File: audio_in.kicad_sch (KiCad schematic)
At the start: 12 parts, among them J4 JST SH3, J5 Header_2x1, U2 OPA1678

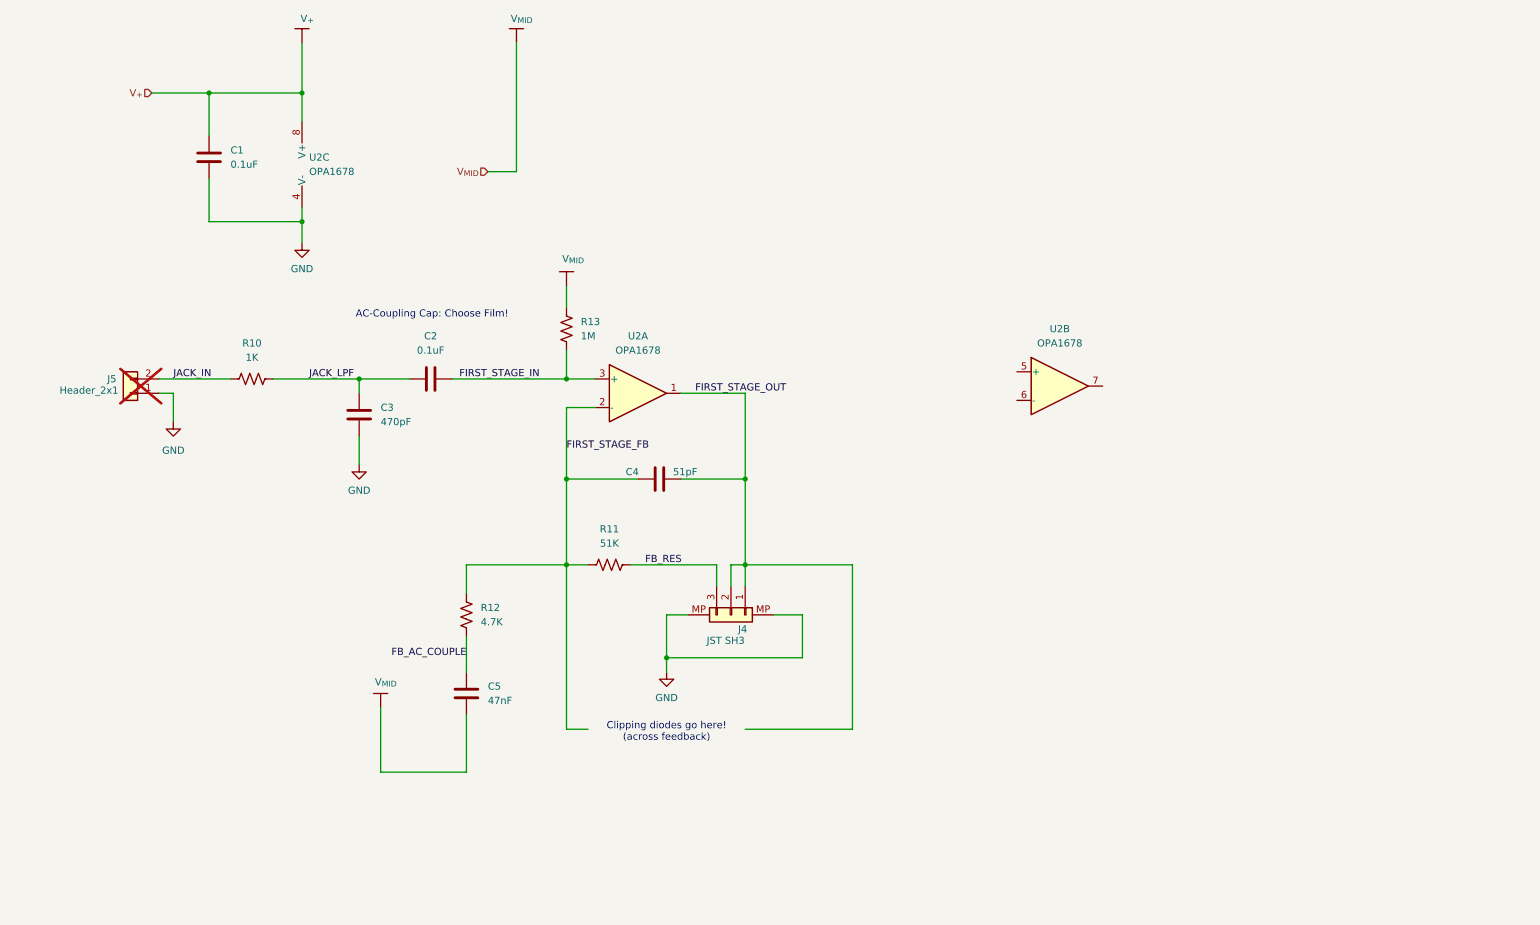
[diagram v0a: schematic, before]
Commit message: Finished second stage, added diode clipping options, and started current buffer.
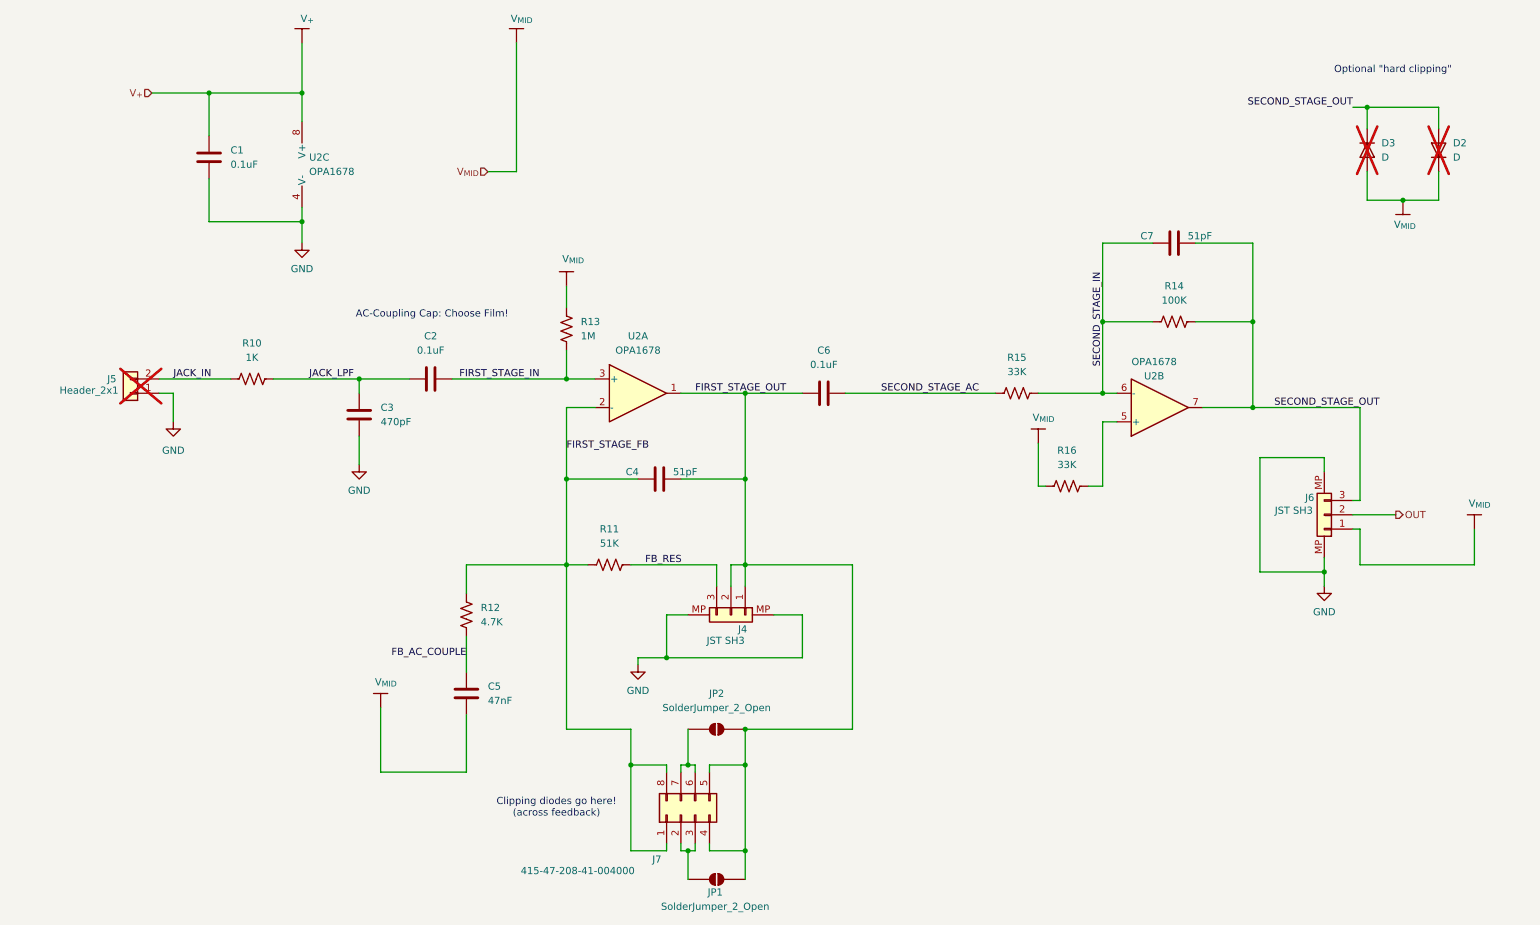
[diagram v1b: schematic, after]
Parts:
- added C6: 0.1uF, Capacitor_SMD:C_1210_3225Metric, symbol #inventree_kicad:C_0U1_PEN_50V_1210
- added C7: 51pF, Capacitor_SMD:C_0402_1005Metric, symbol #inventree_kicad:C_51P_NP0_50V_0402
- added D2, D3: D, symbol Device:D
- added J6: JST SH3, Connector_JST:JST_SH_BM03B-SRSS-TB_1x03-1MP_P1.00mm_Vertical, symbol #inventree_kicad:PWR_CONN_3PIN_JST_SH3_VERT_SMD
- added J7: 415-47-208-41-004000, Connector_PinSocket_2.54mm:PinSocket_2x04_P2.54mm_Vertical, symbol #inventree_kicad:PWR_CONN_8_PIN_SOCKET_THRU
- added JP1, JP2: SolderJumper_2_Open, Jumper:SolderJumper-2_P1.3mm_Open_TrianglePad1.0x1.5mm, symbol Jumper:SolderJumper_2_Open
- added R14: 100K, Resistor_SMD:R_0402_1005Metric, symbol #inventree_kicad:R_100K_0402_1PCT_0W0625
- added R15, R16: 33K, Resistor_SMD:R_0402_1005Metric, symbol #inventree_kicad:R_33K_0402_1PCT_0W0625
- J4: footprint Connector_JST:JST_SH_SM03B-SRSS-TB_1x03-1MP_P1.00mm_Horizontal -> Connector_JST:JST_SH_BM03B-SRSS-TB_1x03-1MP_P1.00mm_Vertical
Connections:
- net FIRST_STAGE_FB: now also J7.1 (Pin_1), J7.8 (Pin_8)
- net FIRST_STAGE_OUT: now also C6.1, J7.4 (Pin_4), J7.5 (Pin_5), JP1.2 (B), JP2.2 (B)
- net GND: now also J6.MP
- net V_{MID}: now also D2.1 (K), D3.2 (A), J6.1 (Pin_1), R16.1
- net at U2.5 (+): now also R16.2
- net SECOND_STAGE_IN: now reaches U2.6 (-)
- net SECOND_STAGE_IN: now also C7.1, R14.1, R15.2
- net SECOND_STAGE_OUT: now reaches U2.7
- net SECOND_STAGE_OUT: now also C7.2, D2.2 (A), D3.1 (K), J6.3 (Pin_3), R14.2
- new net: J7.2 (Pin_2), J7.3 (Pin_3), JP1.1 (A)
- new net: J7.6 (Pin_6), J7.7 (Pin_7), JP2.1 (A)
- new net OUT: J6.2 (Pin_2)
- new net SECOND_STAGE_AC: C6.2, R15.1
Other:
- note added: "Optional "hard clipping""
- moved on the sheet: U2B

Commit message: Added notes and started work on boost converter.
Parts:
- D2, D3: footprint (none) -> Diode_SMD:D_SOD-123
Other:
- note added: "1N4148W-7-F"
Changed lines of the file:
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@@
+		)
+	)
+	(text "1N4148W-7-F"
+		(exclude_from_sim no)
+		(at 246.888 55.88 0)
+		(effects
+			(font
+				(size 1.27 1.27)
+			)
 		)
 	)
@@
 			)
 		)
-		(property "Footprint" ""
+		(property "Footprint" "Diode_SMD:D_SOD-123"
 			(at 271.78 54.61 0)
 			(hide yes)
@@
 			)
 		)
-		(property "Footprint" ""
+		(property "Footprint" "Diode_SMD:D_SOD-123"
 			(at 259.08 54.61 0)
 			(hide yes)

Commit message: Implemented boost stage and now working on schematics for current buffers and rail splitter.
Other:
- title: (none) -> ${PROJECT_NAME}
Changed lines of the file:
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@@
 	(generator_version "10.0")
 	(paper "A4")
+	(title_block
+		(title "${PROJECT_NAME}")
+		(date "2026-08-25")
+		(rev "${REVISION}")
+		(comment 1 "${PCBA_IPN}")
+	)
 	(text "Optional \"hard clipping\""
 		(exclude_from_sim no)

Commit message: Started working on watchdog circuit.
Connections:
- net SECOND_STAGE_OUT renamed WD_AUDIO_OUT
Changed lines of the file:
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@@
+	)
+	(junction
+		(at 257.81 100.33)
+		(diameter 0)
+		(color 0 0 0 0)
 	)
 	(junction
@@
 	(wire
 		(pts
+			(xy 257.81 100.33) (xy 266.7 100.33)
+		)
+		(stroke
+			(width 0)
+			(type default)
+		)
+	)
+	(wire
+		(pts
 			(xy 128.27 163.83) (xy 128.27 157.48)
 		)
@@
 		)
 	)
+	(hierarchical_label "WD_AUDIO_OUT"
+		(shape output)
+		(at 266.7 100.33 0)
+		(effects
+			(font
+				(size 1.27 1.27)
+			)
+			(justify left)
+		)
+	)

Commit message: Small tunes and adjustments before Inventree work.
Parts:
- added FB3: MDF2016BSS600CTD25, Inductor_SMD:L_Wuerth_PMFI-201610, symbol Device:FerriteBead
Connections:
- net V_{+}: now also FB3.1, FB3.2
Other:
- note added: "Av = -R14 / R15 => Av = -100K / 33K = -3.03x"
- note added: "Av = 1 + (R11 + R_pot) / R12 Av_min (R_pot = 0): => Av_min = 1 + 51K/4.7K = 11.9x (21.5 dB) Av_max (R_pot = 500K): => Av_max = 1 + (51K + 500K)/4.7K = 118.2x (41.5 dB)"
- note added: "Gain pot"
- note added: "Volume pot"
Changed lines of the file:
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@@
 	(title_block
 		(title "${PROJECT_NAME}")
-		(date "2026-08-25")
+		(date "2026-08-29")
 		(rev "${REVISION}")
 		(comment 1 "${PCBA_IPN}")
@@
 		)
 	)
+	(text "Gain pot"
+		(exclude_from_sim no)
+		(at 154.94 132.842 0)
+		(effects
+			(font
+				(size 1.27 1.27)
+			)
+		)
+	)
+	(text "Av = -R14 / R15\n=> Av = -100K / 33K = -3.03x"
+		(exclude_from_sim no)
+		(at 197.866 122.174 0)
+		(effects
+			(font
+				(size 1.27 1.27)
+			)
+			(justify left)
+		)
+	)
+	(text "Volume pot"
+		(exclude_from_sim no)
+		(at 265.43 113.284 0)
+		(effects
+			(font
+				(size 1.27 1.27)
+			)
+		)
+	)
 	(text "1N4148W-7-F"
 		(exclude_from_sim no)
@@
 		)
 	)
+	(text "Av = 1 + (R11 + R_pot) / R12\n\nAv_min (R_pot = 0):\n=> Av_min = 1 + 51K/4.7K = 11.9x (21.5 dB)\n\nAv_max (R_pot = 500K):\n=> Av_max = 1 + (51K + 500K)/4.7K = 118.2x (41.5 dB)"
+		(exclude_from_sim no)
+		(at 126.238 67.818 0)
+		(effects
+			(font
+				(size 1.27 1.27)
+			)
+			(justify left)
+		)
+	)
 	(junction
 		(at 116.84 113.03)
@@
 	)
 	(junction
+		(at 53.34 44.45)
+		(diameter 0)
+		(color 0 0 0 0)
+	)
+	(junction
 		(at 116.84 95.25)
 		(diameter 0)
@@
 	)
 	(junction
-		(at 53.34 44.45)
-		(diameter 0)
-		(color 0 0 0 0)
-	)
-	(junction
 		(at 134.62 144.78)
 		(diameter 0)
@@
 	(wire
 		(pts
-			(xy 43.18 44.45) (xy 53.34 44.45)
+			(xy 26.67 44.45) (xy 34.29 44.45)
 		)
 		(stroke
@@
 		(pts
 			(xy 116.84 113.03) (xy 129.54 113.03)
+		)
+		(stroke
+			(width 0)
+			(type default)
+		)
+	)
+	(wire
+		(pts
+			(xy 41.91 44.45) (xy 53.34 44.45)
 		)
 		(stroke
@@
 	(hierarchical_label "V_{+}"
 		(shape input)
-		(at 43.18 44.45 180)
+		(at 26.67 44.45 180)
 		(effects
 			(font
@@
 					(unit 1)
 				)
+			)
+		)
+	)
+	(symbol
+		(lib_id "Device:FerriteBead")
+		(at 38.1 44.45 90)
+		(unit 1)
+		(body_style 1)
+		(exclude_from_sim no)
+		(in_bom yes)
+		(on_board yes)
+		(in_pos_files yes)
+		(dnp no)
+		(fields_autoplaced yes)
+		(property "Reference" "FB3"
+			(at 38.0492 36.83 90)
+			(show_name no)
+			(do_not_autoplace no)
+			(effects
+				(font
+					(size 1.27 1.27)
+				)
+			)
+		)
+		(property "Value" "MDF2016BSS600CTD25"
+			(at 38.0492 39.37 90)
+			(show_name no)
+			(do_not_autoplace no)
+			(effects
+				(font
+					(size 1.27 1.27)
+				)
+			)
+		)
+		(property "Footprint" "Inductor_SMD:L_Wuerth_PMFI-201610"
+			(at 38.1 46.228 90)
+			(hide yes)
+			(show_name no)
+			(do_not_autoplace no)
+			(effects
+				(font
+					(size 1.27 1.27)
+				)
+			)
+		)
+		(property "Datasheet" ""
+			(at 38.1 44.45 0)
+			(hide yes)
+			(show_name no)
+			(do_not_autoplace no)
+			(effects
+				(font
+					(size 1.27 1.27)
+				)
+			)
+		)
+		(property "Description" "Ferrite bead"
+			(at 38.1 44.45 0)
+			(hide yes)
+			(show_name no)
+			(do_not_autoplace no)
+			(effects
+				(font
+					(size 1.27 1.27)
+				)
+			)
+		)
+		(pin "2"
+		)
+		(pin "1"
+		)
+		(instances
+			(project "headphone_amp"
+				(path "/62ffec33-ae93-49a8-bfe6-566578dd8e82/fdaed4ad-6382-4025-bc3e-39eb3bc4a0fb"
+					(reference "FB3")
+					(unit 1)
+				)

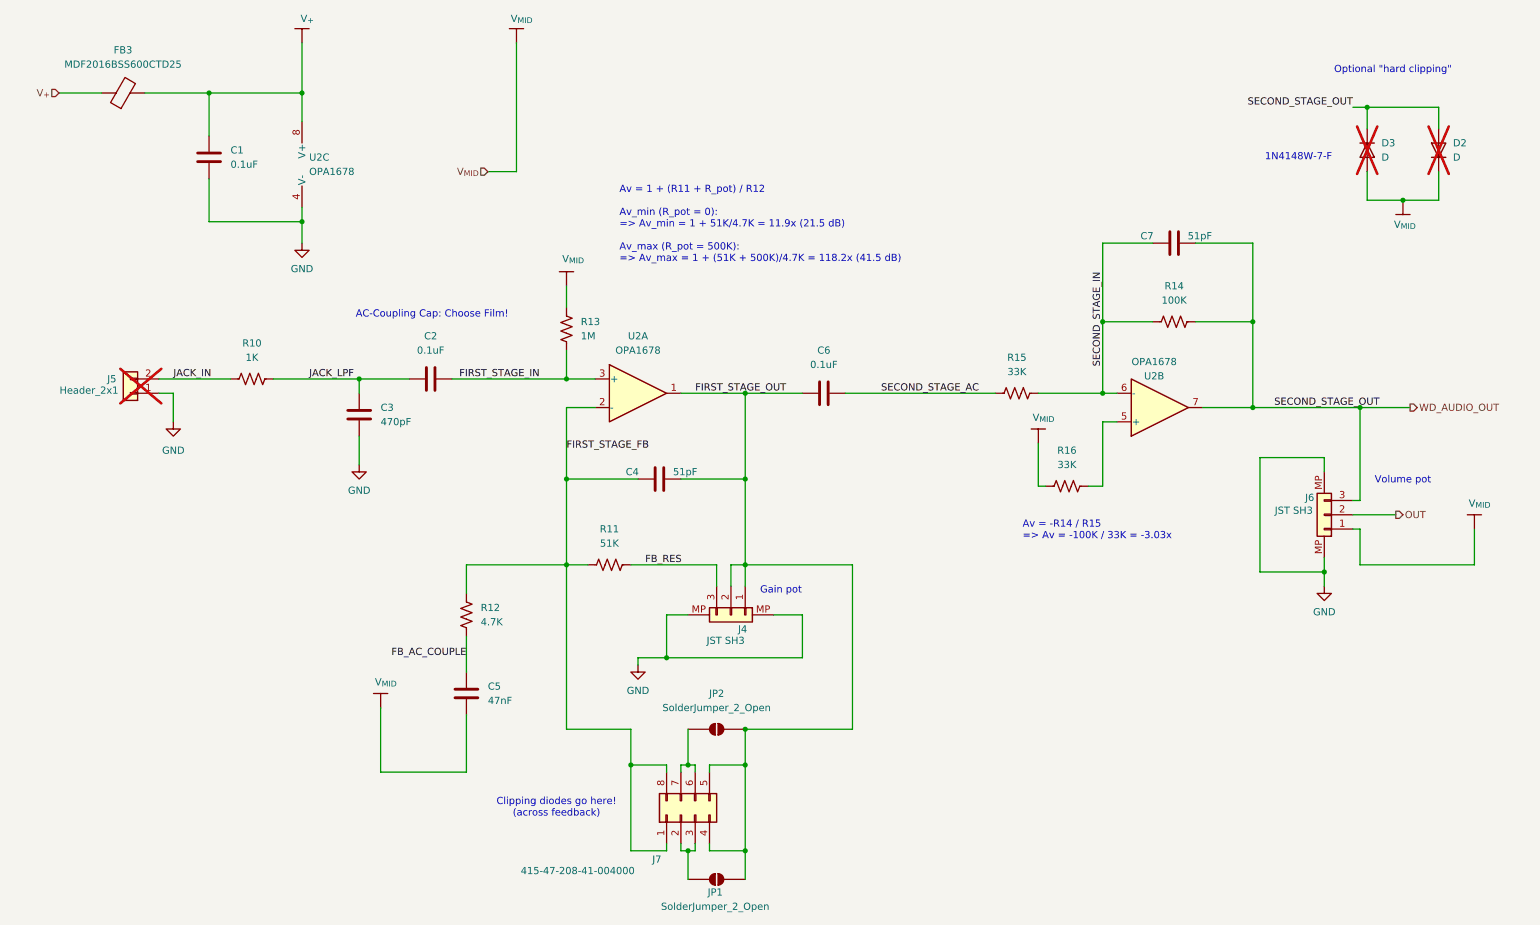
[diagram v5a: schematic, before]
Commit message: Corrected issues Claude identified, added 'poor man's cab filter' on recovery stage per Ihsan.
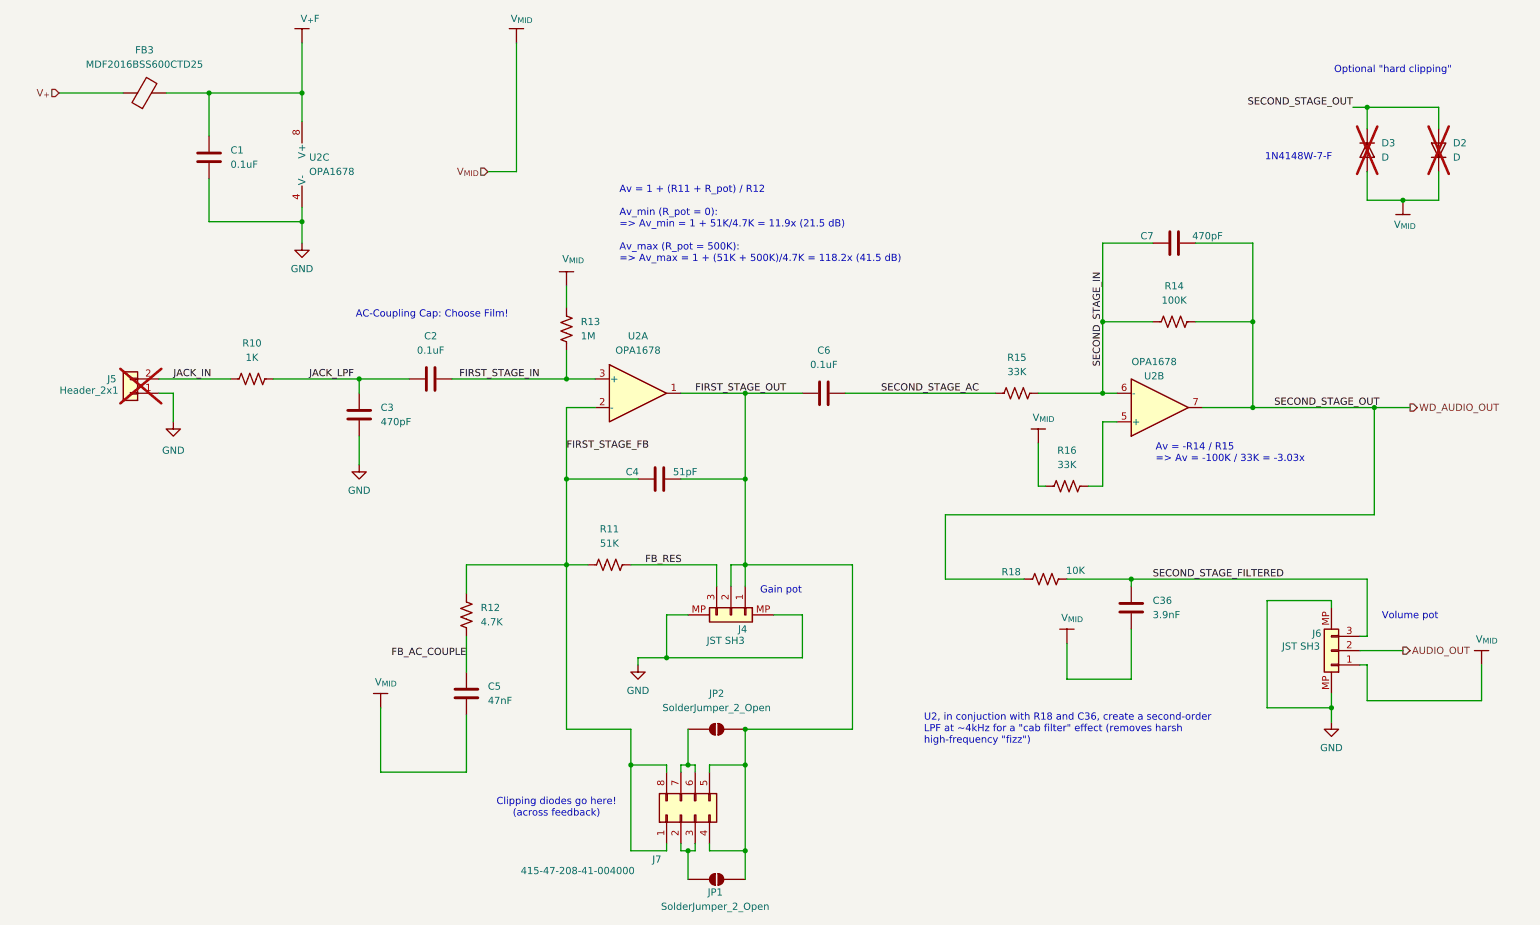
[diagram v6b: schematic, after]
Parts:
- added C36: 3.9nF, Capacitor_SMD:C_0603_1608Metric, symbol inventree_kicad:C_3900P_NP0_50V_0603
- added R18: 10K, Resistor_SMD:R_0402_1005Metric, symbol inventree_kicad:R_10K_0402_1PCT_0W0625
- C7: value 51pF -> 470pF; symbol #inventree_kicad:C_51P_NP0_50V_0402 -> inventree_kicad:C_470P_NP0_50V_0402; IPN 301-0004 -> 301-0002; InvenTree 17 -> 14; Part URL http://10.0.0.33/web/part/17/ -> http://10.0.0.33/web/part/14/
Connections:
- net V_{+}: no longer C1.1, FB3.2, U2.8 (V+)
- net V_{MID}: now also C36.2
- net WD_AUDIO_OUT: now also R18.1; no longer J6.3 (Pin_3)
- net OUT renamed AUDIO_OUT
- new net SECOND_STAGE_FILTERED: C36.1, J6.3 (Pin_3), R18.2
- new net V_{+}F: C1.1, FB3.2, U2.8 (V+)
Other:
- note added: "U2, in conjuction with R18 and C36, create a second-order LPF at ~4kHz for a "cab filter" effect (removes harsh high-frequency "fizz")"
- moved on the sheet: FB3
